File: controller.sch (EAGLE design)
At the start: 27 parts, among them U1 10118194-MICRO-USB, U2 LM3671MF-3.3/NOPBMF05A-M, U3 SN74LVC1T45DBVRDBV6-M, U4 SN74LVC1T45DBVRDBV6-M, U5 SS8050-G, U6 SS8050-G

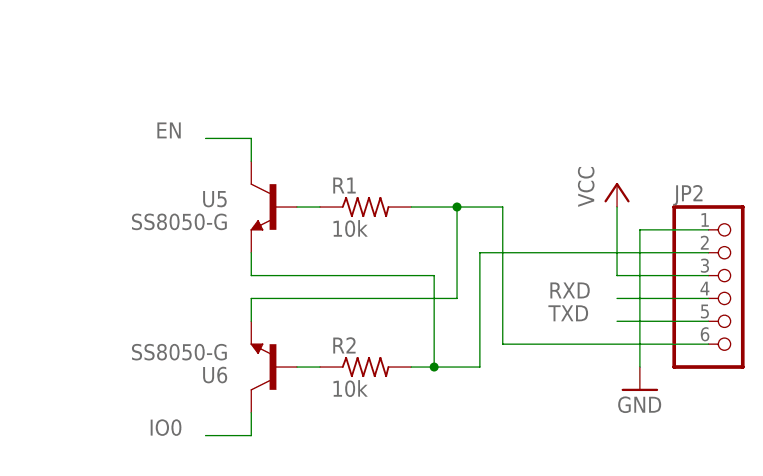
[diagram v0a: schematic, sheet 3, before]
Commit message: Fixed a bunch of bugs in v1.0
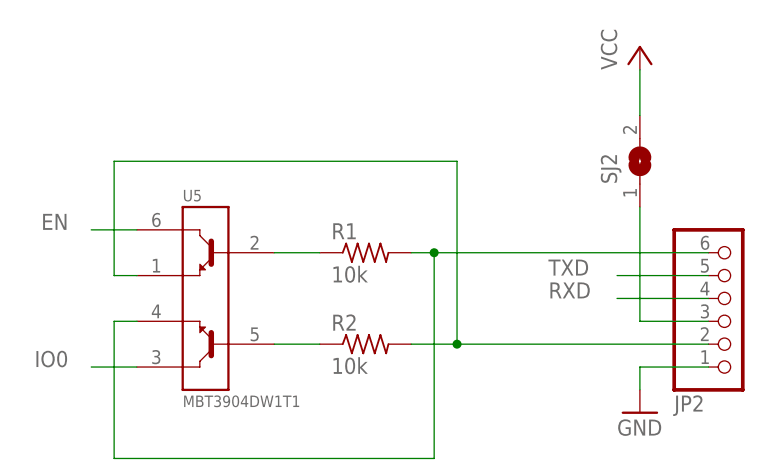
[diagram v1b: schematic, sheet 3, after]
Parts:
- removed U6: SS8050-G, nebrius:SS8050-G
- added C3: 0.1uF, rcl:C-USC0805
- added R7: (no value), rcl:R-US_R0805
- added SJ2: (no value), jumper:SJ
- R6: value 220 -> 1k
- U5: value SS8050-G -> MBT3904DW1T1; device nebrius:SS8050-G -> nebrius:MBT3904DW1T1
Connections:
- new net N$11: JP2.3, SJ2.1
- net +5V: no longer JP7.2
- net EN: now also C3.1, U5.C2; no longer U5.C
- net GND: now also C3.2, JP7.2
- net IO0: now also R7.1, U5.C1; no longer U6.C
- net N$12: now also JP2.2, R2.2, U5.E2; no longer JP2.6, R1.2, U6.E
- net N$4: now also U5.B2; no longer U5.B
- net N$5: now also U5.B1; no longer U6.B
- net N$6: now also JP2.6, R1.2, U5.E1; no longer JP2.2, R2.2, U5.E
- net VCC: now also R7.2, SJ2.2; no longer JP2.3
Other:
- moved on the sheet: JP2, R1, R2, R3

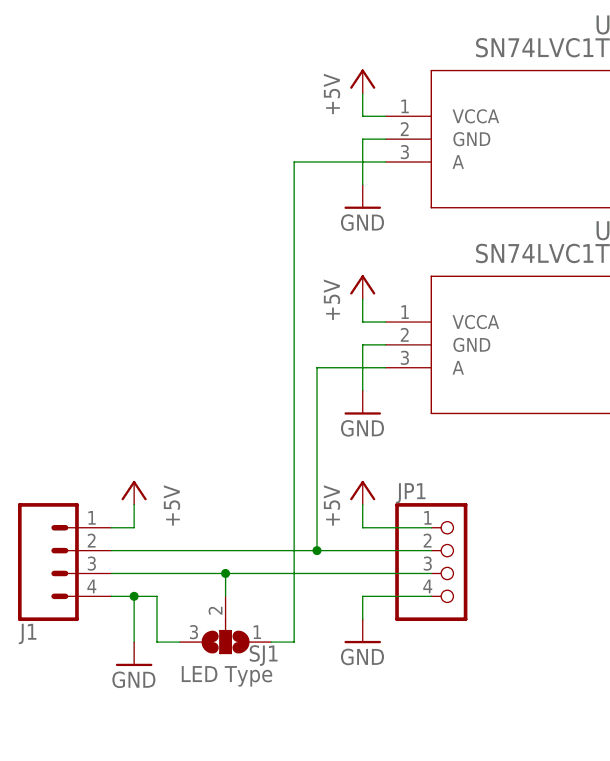
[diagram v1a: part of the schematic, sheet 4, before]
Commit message: Tweaks and bug fixes from v1.1 board
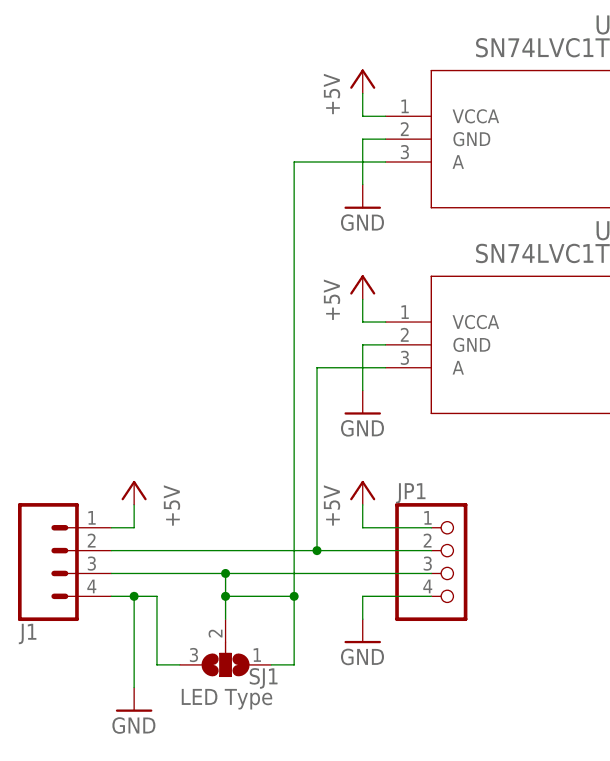
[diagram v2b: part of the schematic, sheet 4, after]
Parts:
- removed C3: 0.1uF, rcl:C-USC0805
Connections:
- removed net N$11: JP2.3, SJ2.1
- removed net N$8: SJ1.1, U3.A
- net DOWN: now also R5.4, S1.UP, U$2.IO19; no longer R5.1, S1.DOWN, U$2.IO5
- net EN: no longer C3.1
- net GND: no longer C3.2
- net N$7: now also SJ1.1, U3.A
- net UP: now also R5.1, S1.DOWN, U$2.IO5; no longer R5.4, S1.UP, U$2.IO19
- net VCC: now also JP2.3, SJ2.1
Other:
- note added: "Note: UP/DOWN are backwards in the part library for the joystick"
- moved on the sheet: SJ1
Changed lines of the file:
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@@
 <?xml version="1.0" encoding="utf-8"?>
 <!DOCTYPE eagle SYSTEM "eagle.dtd">
-<eagle version="9.5.1">
+<eagle version="9.5.2">
 <drawing>
 <settings>
@@
 <part name="P+15" library="supply1" library_urn="urn:adsk.eagle:library:371" deviceset="VCC" device=""/>
 <part name="U5" library="nebrius" deviceset="MBT3904DW1T1" device=""/>
-<part name="C3" library="rcl" library_urn="urn:adsk.eagle:library:334" deviceset="C-US" device="C0805" package3d_urn="urn:adsk.eagle:package:23617/2" value="0.1uF"/>
-<part name="GND22" library="supply1" library_urn="urn:adsk.eagle:library:371" deviceset="GND" device=""/>
 <part name="P+16" library="supply1" library_urn="urn:adsk.eagle:library:371" deviceset="VCC" device=""/>
 <part name="SJ2" library="jumper" library_urn="urn:adsk.eagle:library:252" deviceset="SJ" device="" package3d_urn="urn:adsk.eagle:package:15471/1"/>
@@
 <attribute name="VALUE" x="63.5" y="0" size="1.778" layer="96" rot="R90"/>
 </instance>
-<instance part="C3" gate="G$1" x="-55.88" y="7.62" smashed="yes">
-<attribute name="NAME" x="-54.864" y="8.255" size="1.778" layer="95"/>
-<attribute name="VALUE" x="-54.864" y="3.429" size="1.778" layer="96"/>
-</instance>
-<instance part="GND22" gate="1" x="-55.88" y="-2.54" smashed="yes">
-<attribute name="VALUE" x="-58.42" y="-5.08" size="1.778" layer="96"/>
-</instance>
 <instance part="P+16" gate="VCC" x="-55.88" y="30.48" smashed="yes">
 <attribute name="VALUE" x="-58.42" y="27.94" size="1.778" layer="96" rot="R90"/>
@@
 <wire x1="-12.7" y1="-22.86" x2="-12.7" y2="-27.94" width="0.1524" layer="91"/>
 <pinref part="U$2" gate="G$1" pin="GND@3"/>
-</segment>
-<segment>
-<pinref part="GND22" gate="1" pin="GND"/>
-<pinref part="C3" gate="G$1" pin="2"/>
-<wire x1="-55.88" y1="0" x2="-55.88" y2="2.54" width="0.1524" layer="91"/>
 </segment>
 </net>
@@
 <pinref part="U$2" gate="G$1" pin="EN"/>
 <label x="-63.5" y="12.7" size="1.778" layer="95" align="bottom-right"/>
-<pinref part="C3" gate="G$1" pin="1"/>
-<wire x1="-55.88" y1="12.7" x2="-55.88" y2="10.16" width="0.1524" layer="91"/>
 </segment>
 </net>
@@
 </segment>
 </net>
-<net name="DOWN" class="0">
+<net name="UP" class="0">
 <segment>
 <pinref part="U$2" gate="G$1" pin="IO5"/>
@@
 </segment>
 </net>
-<net name="UP" class="0">
+<net name="DOWN" class="0">
 <segment>
 <pinref part="U$2" gate="G$1" pin="IO19"/>
@@
 <pinref part="P+14" gate="VCC" pin="VCC"/>
 <pinref part="SJ2" gate="1" pin="2"/>
-<wire x1="71.12" y1="68.58" x2="71.12" y2="73.66" width="0.1524" layer="91"/>
-</segment>
-</net>
-<net name="N$11" class="0">
-<segment>
+<wire x1="71.12" y1="68.58" x2="71.12" y2="71.12" width="0.1524" layer="91"/>
 <pinref part="JP2" gate="A" pin="3"/>
+<wire x1="71.12" y1="71.12" x2="71.12" y2="73.66" width="0.1524" layer="91"/>
 <wire x1="78.74" y1="45.72" x2="71.12" y2="45.72" width="0.1524" layer="91"/>
 <pinref part="SJ2" gate="1" pin="1"/>
-<wire x1="71.12" y1="58.42" x2="71.12" y2="45.72" width="0.1524" layer="91"/>
+<wire x1="71.12" y1="58.42" x2="71.12" y2="55.88" width="0.1524" layer="91"/>
+<wire x1="71.12" y1="55.88" x2="71.12" y2="45.72" width="0.1524" layer="91"/>
+<wire x1="71.12" y1="55.88" x2="73.66" y2="55.88" width="0.1524" layer="91"/>
+<junction x="71.12" y="55.88"/>
+<wire x1="73.66" y1="55.88" x2="73.66" y2="71.12" width="0.1524" layer="91"/>
+<wire x1="73.66" y1="71.12" x2="71.12" y2="71.12" width="0.1524" layer="91"/>
+<junction x="71.12" y="71.12"/>
 </segment>
 </net>
@@
 <attribute name="NAME" x="-22.86" y="45.212" size="1.778" layer="95" font="vector" rot="MR180"/>
 </instance>
-<instance part="GND17" gate="1" x="-10.16" y="40.64" smashed="yes">
-<attribute name="VALUE" x="-12.7" y="38.1" size="1.778" layer="96"/>
-</instance>
-<instance part="SJ1" gate="G$1" x="0" y="43.18" smashed="yes" rot="R270">
-<attribute name="NAME" x="2.54" y="41.021" size="1.778" layer="95"/>
-<attribute name="VALUE" x="-5.08" y="38.735" size="1.778" layer="96"/>
+<instance part="GND17" gate="1" x="-10.16" y="35.56" smashed="yes">
+<attribute name="VALUE" x="-12.7" y="33.02" size="1.778" layer="96"/>
+</instance>
+<instance part="SJ1" gate="G$1" x="0" y="40.64" smashed="yes" rot="R270">
+<attribute name="NAME" x="2.54" y="38.481" size="1.778" layer="95"/>
+<attribute name="VALUE" x="-5.08" y="36.195" size="1.778" layer="96"/>
 </instance>
 <instance part="JP1" gate="A" x="25.4" y="50.8" smashed="yes">
@@
 <segment>
 <pinref part="GND17" gate="1" pin="GND"/>
-<wire x1="-10.16" y1="48.26" x2="-10.16" y2="43.18" width="0.1524" layer="91"/>
+<wire x1="-10.16" y1="48.26" x2="-10.16" y2="38.1" width="0.1524" layer="91"/>
 <pinref part="J1" gate="G$1" pin="4"/>
 <wire x1="-12.7" y1="48.26" x2="-10.16" y2="48.26" width="0.1524" layer="91"/>
-<wire x1="-5.08" y1="43.18" x2="-7.62" y2="43.18" width="0.1524" layer="91"/>
-<wire x1="-7.62" y1="43.18" x2="-7.62" y2="48.26" width="0.1524" layer="91"/>
+<wire x1="-5.08" y1="40.64" x2="-7.62" y2="40.64" width="0.1524" layer="91"/>
+<wire x1="-7.62" y1="40.64" x2="-7.62" y2="48.26" width="0.1524" layer="91"/>
 <wire x1="-7.62" y1="48.26" x2="-10.16" y2="48.26" width="0.1524" layer="91"/>
 <junction x="-10.16" y="48.26"/>
@@
 <wire x1="73.66" y1="78.74" x2="76.2" y2="78.74" width="0.1524" layer="91"/>
 <wire x1="76.2" y1="78.74" x2="76.2" y2="81.28" width="0.1524" layer="91"/>
-</segment>
-</net>
-<net name="N$8" class="0">
-<segment>
-<pinref part="U3" gate="A" pin="A"/>
-<wire x1="7.62" y1="96.52" x2="17.78" y2="96.52" width="0.1524" layer="91"/>
-<wire x1="7.62" y1="96.52" x2="7.62" y2="43.18" width="0.1524" layer="91"/>
-<wire x1="7.62" y1="43.18" x2="5.08" y2="43.18" width="0.1524" layer="91"/>
-<pinref part="SJ1" gate="G$1" pin="1"/>
 </segment>
 </net>
@@
 <net name="N$7" class="0">
 <segment>
+<wire x1="0" y1="45.72" x2="0" y2="48.26" width="0.1524" layer="91"/>
 <wire x1="0" y1="48.26" x2="0" y2="50.8" width="0.1524" layer="91"/>
 <wire x1="0" y1="50.8" x2="22.86" y2="50.8" width="0.1524" layer="91"/>
@@
 <pinref part="SJ1" gate="G$1" pin="2"/>
 <pinref part="JP1" gate="A" pin="3"/>
+<pinref part="U3" gate="A" pin="A"/>
+<wire x1="7.62" y1="96.52" x2="17.78" y2="96.52" width="0.1524" layer="91"/>
+<wire x1="7.62" y1="96.52" x2="7.62" y2="48.26" width="0.1524" layer="91"/>
+<wire x1="7.62" y1="48.26" x2="7.62" y2="40.64" width="0.1524" layer="91"/>
+<wire x1="7.62" y1="40.64" x2="5.08" y2="40.64" width="0.1524" layer="91"/>
+<pinref part="SJ1" gate="G$1" pin="1"/>
+<wire x1="0" y1="48.26" x2="7.62" y2="48.26" width="0.1524" layer="91"/>
+<junction x="0" y="48.26"/>
+<junction x="7.62" y="48.26"/>
 </segment>
 </net>
@@
 <description>UI</description>
 <plain>
+<text x="35.56" y="25.4" size="1.778" layer="97">Note: UP/DOWN are backwards in the part library for the joystick</text>
 </plain>
 <instances>
@@
 </segment>
 </net>
-<net name="UP" class="0">
+<net name="DOWN" class="0">
 <segment>
 <pinref part="S1" gate="G$1" pin="UP"/>
@@
 </segment>
 </net>
-<net name="DOWN" class="0">
+<net name="UP" class="0">
 <segment>
 <pinref part="S1" gate="G$1" pin="DOWN"/>

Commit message: Made a lot of progress with redesign
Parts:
- removed F1: FUSE-0805, nebrius:FUSE-0805
- removed JP3: JTAG, pinhead:PINHD-2X3
- removed JP7: GPIO, pinhead:PINHD-2X5
- removed R1, R2: 10k, rcl:R-US_R0805
- removed U$3: CL-SA-12C4, nebrius:CL-SA-12C4
- removed U5: MBT3904DW1T1, nebrius:MBT3904DW1T1
- added S2, S3: (no value), SparkFun-Switches:MOMENTARY-SWITCH-SPST-2-SMD-4.6X2.8MM
- JP2: value FTDI -> (none); device pinhead:PINHD-1X6 -> pinhead:PINHD-2X8
- R7: value (none) -> 10k
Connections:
- removed net N$12: JP2.2, R2.2, U5.E2
- removed net N$4: R1.1, U5.B2
- removed net N$5: R2.1, U5.B1
- removed net N$6: JP2.6, R1.2, U5.E1
- net +5V: no longer F1.1, U$3.2
- net EN: now also JP2.11, S3.3, S3.4; no longer JP3.1, U5.C2
- net GND: now also S2.3, S2.4, S3.1, S3.2; no longer JP2.1, JP3.6, JP7.10, JP7.2
- net GPIO16: now also JP2.4; no longer JP7.4
- net GPIO17: now also JP2.6; no longer JP7.6
- net GPIO25: now also JP2.7; no longer JP7.7
- net GPIO26: now also JP2.9; no longer JP7.9
- net GPIO27: now also JP2.8; no longer JP7.8
- net GPIO32: now also JP2.3; no longer JP7.3
- net GPIO33: now also JP2.5; no longer JP7.5
- net IO0: now also S2.1, S2.2; no longer U5.C1
- net N$2: now also JP2.2; no longer U$3.3, U1.5V
- net N$3: now also U1.5V; no longer F1.2
- net RXD: now also JP2.12; no longer JP2.4
- net TCK: now also JP2.13; no longer JP3.3
- net TDI: now also JP2.16; no longer JP3.4
- net TDO: now also JP2.14; no longer JP3.2
- net TMS: now also JP2.15; no longer JP3.5
- net TXD: now also JP2.10; no longer JP2.5
- net VCC: now also JP2.1; no longer JP2.3, JP7.1

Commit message: Finished v1.2
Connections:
- removed net N$2: JP2.2
- removed net N$3: C1.1, U1.5V, U2.EN, U2.VIN
- net +5V: now also C1.1, U1.5V, U2.EN, U2.VIN
- net GND: now also JP2.2
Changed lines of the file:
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@@
 </segment>
 </net>
-<net name="N$3" class="0">
+<net name="+5V" class="0">
 <segment>
 <pinref part="U2" gate="A" pin="VIN"/>
@@
 </segment>
 </net>
-<net name="N$2" class="0">
+<net name="GND" class="0">
 <segment>
 <wire x1="73.66" y1="101.6" x2="81.28" y2="101.6" width="0.1524" layer="91"/>

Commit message: Version 1.3
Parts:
- added SJ3: (no value), jumper:SJ
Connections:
- net +5V: now also SJ3.1, SJ3.2
- net EN: no longer JP2.11
- net GND: now also JP2.11

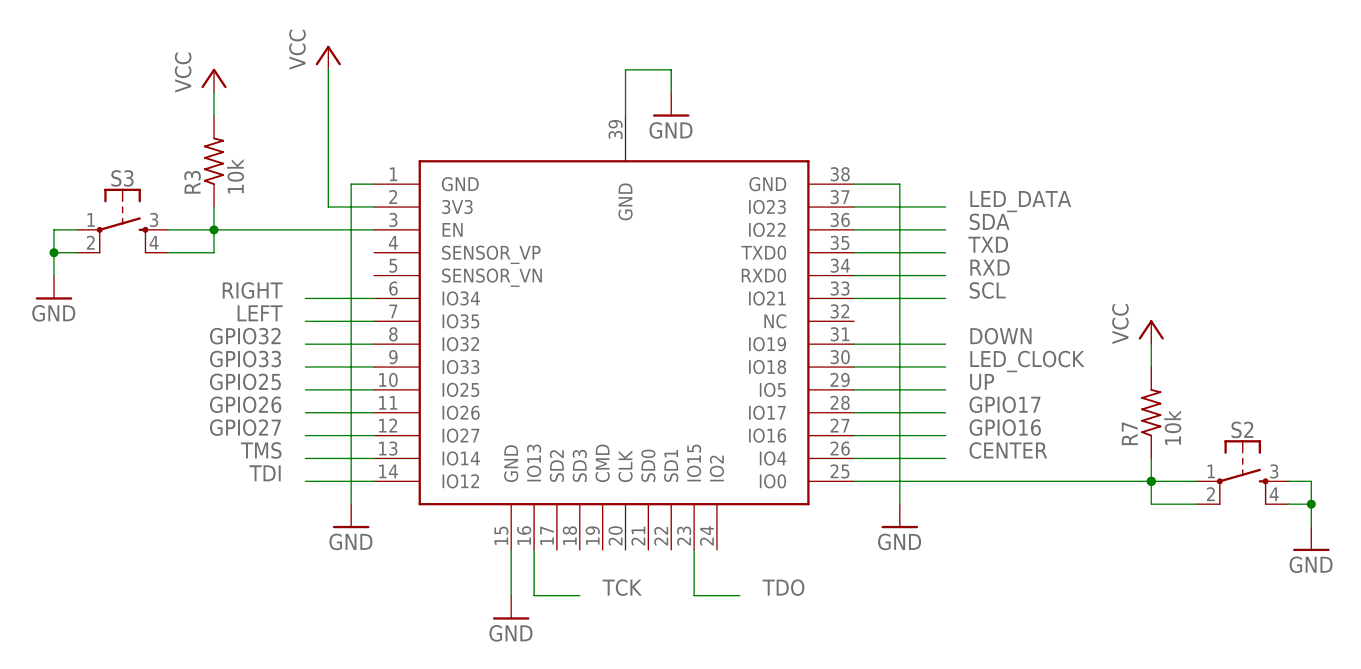
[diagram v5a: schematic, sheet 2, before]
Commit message: Fixed pin labelling
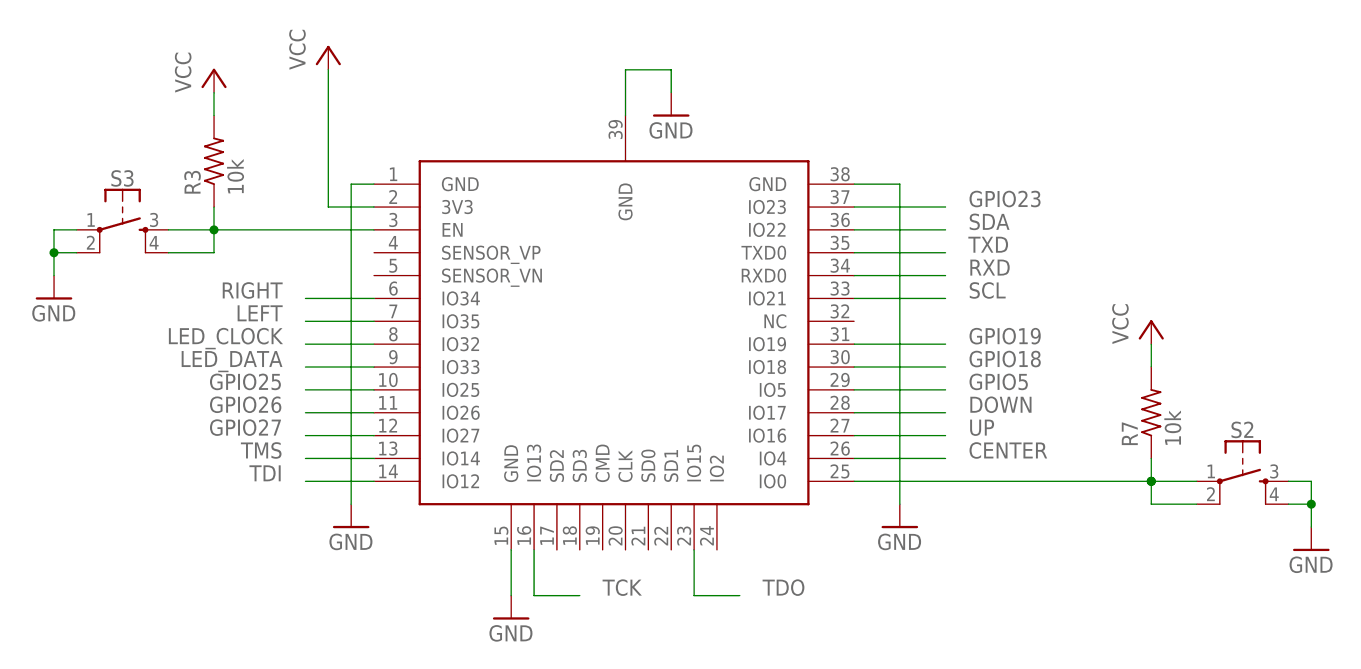
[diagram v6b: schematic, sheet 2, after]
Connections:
- removed net GPIO16: JP2.4, U$2.IO16
- removed net GPIO17: JP2.6, U$2.IO17
- removed net GPIO32: JP2.3, U$2.IO32
- removed net GPIO33: JP2.5, U$2.IO33
- new net GPIO18: JP2.5, U$2.IO18
- new net GPIO19: JP2.4, U$2.IO19
- new net GPIO23: JP2.3, U$2.IO23
- new net GPIO5: JP2.6, U$2.IO5
- net DOWN: now also U$2.IO17; no longer U$2.IO19
- net LED_CLOCK: now also U$2.IO32; no longer U$2.IO18
- net LED_DATA: now also U$2.IO33; no longer U$2.IO23
- net UP: now also U$2.IO16; no longer U$2.IO5
